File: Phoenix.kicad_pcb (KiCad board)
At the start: 2 copper layers, 83.2 x 37.6 mm, 88 parts, among them J1 Mini USB Female, J2 Battery Connector, J3 Pyro Connectors, Q1 2N7000, Q2 BSS84, Q3 IRFML8244TRPBF, Q4 IRFML8244TRPBF, Q5 IRFML8244TRPBF, Q6 IRFML8244TRPBF, U1 RP2040, U3 AMS1117-3.3, U4 I3G4250D, U5 MS5637-02BA03, U6 ADXL343, U8 Si4468/7, U9 L70B-M39, Y1 12MHz, Y2 30MHz

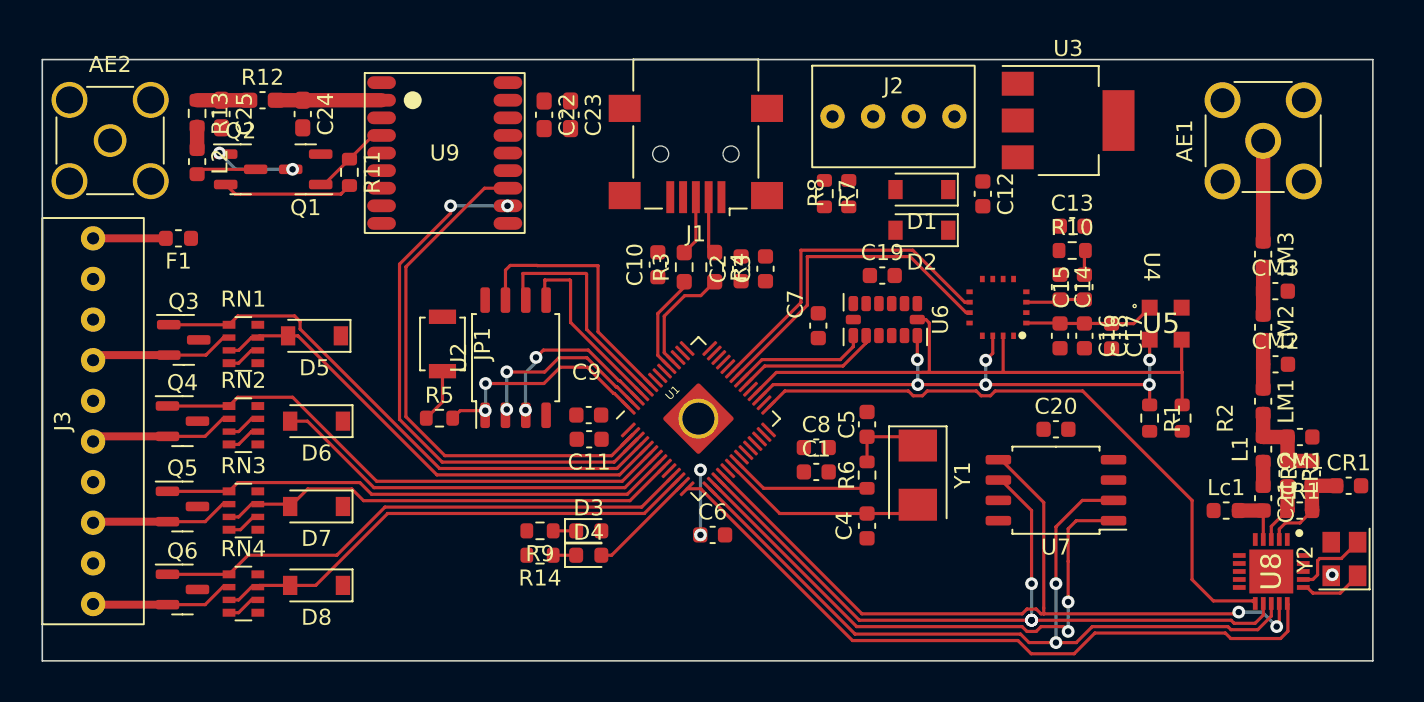
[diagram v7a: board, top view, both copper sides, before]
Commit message: Added fills
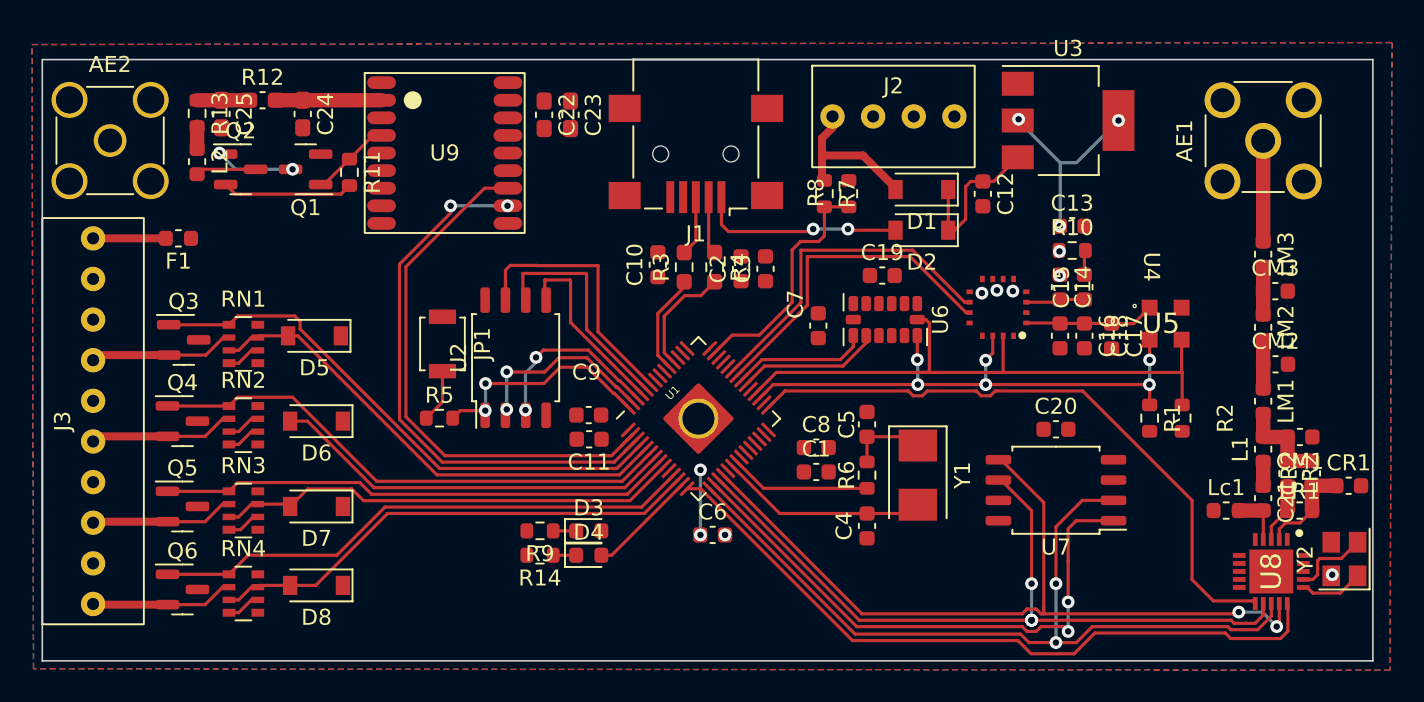
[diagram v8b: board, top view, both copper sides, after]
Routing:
- net /Power Supply/VBat/4: track 0.00 -> 15.6 mm
- net VBUS: track 0.00 -> 12.9 mm, vias 0 -> 2
- net +3V3: track 4.08 -> 16.9 mm, vias 2 -> 5
- net Net-(C12-Pad1): track 0.00 -> 9.97 mm
- net +BATT: track 0.00 -> 9.92 mm
- net GND: vias 1 -> 7
- added copper zone on B.Cu, net GND
- added copper zone on F.Cu, net GND
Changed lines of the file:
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@@
   (segment (start 139.446 37.1915) (end 139.446 30.8925) (width 0.9) (layer "F.Cu") (net 1))
   (segment (start 76.025 28.3545) (end 72.797 28.3545) (width 0.9) (layer "F.Cu") (net 2))
+  (via (at 126.711526 37.80667) (size 0.8) (drill 0.4) (layers "F.Cu" "B.Cu") (net 4))
+  (via (at 121.861299 40.415582) (size 0.8) (drill 0.4) (layers "F.Cu" "B.Cu") (free) (net 4))
   (via (at 143.764 58.0195) (size 0.8) (drill 0.4) (layers "F.Cu" "B.Cu") (net 4))
+  (via (at 126.723013 39.323004) (size 0.8) (drill 0.4) (layers "F.Cu" "B.Cu") (net 4))
+  (via (at 122.800711 40.236889) (size 0.8) (drill 0.4) (layers "F.Cu" "B.Cu") (free) (net 4))
+  (via (at 123.796284 40.287944) (size 0.8) (drill 0.4) (layers "F.Cu" "B.Cu") (free) (net 4))
+  (via (at 105.804 55.5305) (size 0.8) (drill 0.4) (layers "F.Cu" "B.Cu") (free) (net 4))
   (segment (start 104.254 55.5305) (end 104.267 55.5305) (width 0.2) (layer "F.Cu") (net 5))
+  (segment (start 126.537926 36.031426) (end 126.733 36.2265) (width 0.2) (layer "F.Cu") (net 5))
+  (via (at 126.733 36.2265) (size 0.8) (drill 0.4) (layers "F.Cu" "B.Cu") (net 5))
+  (via (at 130.404 29.6225) (size 0.8) (drill 0.4) (layers "F.Cu" "B.Cu") (net 5))
+  (via (at 124.155693 29.544612) (size 0.8) (drill 0.4) (layers "F.Cu" "B.Cu") (net 5))
   (via (at 104.267 55.5305) (size 0.8) (drill 0.4) (layers "F.Cu" "B.Cu") (net 5))
   (via (at 104.267 51.4665) (size 0.8) (drill 0.4) (layers "F.Cu" "B.Cu") (net 5))
+  (segment (start 126.761241 32.259746) (end 127.766754 32.259746) (width 0.2) (layer "B.Cu") (net 5))
+  (segment (start 124.155693 29.544612) (end 124.155693 29.654198) (width 0.2) (layer "B.Cu") (net 5))
+  (segment (start 124.155693 29.654198) (end 126.761241 32.259746) (width 0.2) (layer "B.Cu") (net 5))
   (segment (start 104.267 55.5305) (end 104.267 51.4665) (width 0.2) (layer "B.Cu") (net 5))
+  (segment (start 126.761241 36.198259) (end 126.733 36.2265) (width 0.2) (layer "B.Cu") (net 5))
+  (segment (start 127.766754 32.259746) (end 130.404 29.6225) (width 0.2) (layer "B.Cu") (net 5))
+  (segment (start 126.761241 32.259746) (end 126.761241 36.198259) (width 0.2) (layer "B.Cu") (net 5))
   (segment (start 114.681 54.1925) (end 109.223972 54.1925) (width 0.2) (layer "F.Cu") (net 6))
   (segment (start 117.306 54.1925) (end 114.681 54.1925) (width 0.2) (layer "F.Cu") (net 6))
@@
   (segment (start 140.9705 50.907) (end 140.97 50.9075) (width 0.9) (layer "F.Cu") (net 8))
   (segment (start 142.494 50.907) (end 140.9705 50.907) (width 0.9) (layer "F.Cu") (net 8))
+  (segment (start 112.522 29.3685) (end 112.522 30.070541) (width 0.5) (layer "F.Cu") (net 9))
+  (segment (start 116.46 33.838447) (end 114.429233 31.80768) (width 0.5) (layer "F.Cu") (net 9))
+  (segment (start 111.999651 31.80768) (end 111.870419 31.936912) (width 0.5) (layer "F.Cu") (net 9))
+  (segment (start 114.429233 31.80768) (end 111.999651 31.80768) (width 0.5) (layer "F.Cu") (net 9))
+  (segment (start 111.870419 31.936912) (end 111.870419 33.225919) (width 0.5) (layer "F.Cu") (net 9))
+  (segment (start 116.46 33.9405) (end 116.46 33.838447) (width 0.5) (layer "F.Cu") (net 9))
+  (segment (start 111.870419 30.722122) (end 111.870419 31.936912) (width 0.5) (layer "F.Cu") (net 9))
+  (segment (start 112.522 30.070541) (end 111.870419 30.722122) (width 0.5) (layer "F.Cu") (net 9))
+  (segment (start 111.870419 33.225919) (end 112.014 33.3695) (width 0.5) (layer "F.Cu") (net 9))
+  (segment (start 111.15942 36.563455) (end 106.018186 36.563455) (width 0.2) (layer "F.Cu") (net 10))
+  (segment (start 116.46 36.4805) (end 113.559098 36.4805) (width 0.2) (layer "F.Cu") (net 10))
+  (segment (start 111.3145 36.408375) (end 111.15942 36.563455) (width 0.2) (layer "F.Cu") (net 10))
+  (segment (start 106.018186 36.563455) (end 105.578499 36.123768) (width 0.2) (layer "F.Cu") (net 10))
+  (segment (start 105.578499 36.123768) (end 105.578499 34.4135) (width 0.2) (layer "F.Cu") (net 10))
+  (segment (start 113.559098 36.4805) (end 113.486973 36.408375) (width 0.2) (layer "F.Cu") (net 10))
+  (via (at 111.3145 36.408375) (size 0.8) (drill 0.4) (layers "F.Cu" "B.Cu") (net 10))
+  (via (at 113.486973 36.408375) (size 0.8) (drill 0.4) (layers "F.Cu" "B.Cu") (net 10))
+  (segment (start 113.486973 36.408375) (end 111.3145 36.408375) (width 0.2) (layer "B.Cu") (net 10))
   (segment (start 95.059 55.2765) (end 96.4945 55.2765) (width 0.2) (layer "F.Cu") (net 11))
   (segment (start 105.156 37.8775) (end 104.778499 37.499999) (width 0.2) (layer "F.Cu") (net 12))
@@
   (segment (start 81.534 56.8005) (end 75.986 56.8005) (width 0.2) (layer "F.Cu") (net 51))
   (segment (start 102.584365 51.795534) (end 100.589399 53.7905) (width 0.2) (layer "F.Cu") (net 51))
+  (segment (start 109.997837 40.987949) (end 107.945472 43.040314) (width 0.2) (layer "F.Cu") (net 54))
+  (segment (start 112.014 35.0195) (end 112.014 36.834562) (width 0.2) (layer "F.Cu") (net 54))
+  (segment (start 112.014 36.834562) (end 111.662504 37.186058) (width 0.2) (layer "F.Cu") (net 54))
+  (segment (start 112.014 35.0195) (end 113.538 35.0195) (width 0.2) (layer "F.Cu") (net 54))
+  (segment (start 110.525709 37.186058) (end 109.997837 37.71393) (width 0.2) (layer "F.Cu") (net 54))
+  (segment (start 111.662504 37.186058) (end 110.525709 37.186058) (width 0.2) (layer "F.Cu") (net 54))
+  (segment (start 109.997837 37.71393) (end 109.997837 40.987949) (width 0.2) (layer "F.Cu") (net 54))
+  (segment (start 107.945472 43.040314) (end 106.248416 43.040314) (width 0.2) (layer "F.Cu") (net 54))
+  (segment (start 106.248416 43.040314) (end 104.839614 44.449116) (width 0.2) (layer "F.Cu") (net 54))
   (segment (start 74.792 43.9925) (end 75.392 43.9925) (width 0.2) (layer "F.Cu") (net 59))
   (segment (start 75.392 43.9925) (end 76.192 43.1925) (width 0.2) (layer "F.Cu") (net 59))
@@
   (segment (start 124.64 40.9815) (end 126.576 40.9815) (width 0.2) (layer "F.Cu") (net 81))
   (segment (start 126.576 40.9815) (end 126.746 40.8115) (width 0.2) (layer "F.Cu") (net 81))
+  (segment (start 121.92 33.4325) (end 122.594 33.4325) (width 0.2) (layer "F.Cu") (net 82))
+  (segment (start 119.76 36.4805) (end 120.158845 36.4805) (width 0.2) (layer "F.Cu") (net 82))
+  (segment (start 121.162092 33.4325) (end 121.92 33.4325) (width 0.2) (layer "F.Cu") (net 82))
+  (segment (start 119.76 36.4805) (end 119.76 33.9405) (width 0.2) (layer "F.Cu") (net 82))
+  (segment (start 120.158845 36.4805) (end 120.848089 35.791256) (width 0.2) (layer "F.Cu") (net 82))
+  (segment (start 122.594 33.4325) (end 124.104 31.9225) (width 0.2) (layer "F.Cu") (net 82))
+  (segment (start 120.848089 35.791256) (end 120.848089 33.746503) (width 0.2) (layer "F.Cu") (net 82))
+  (segment (start 120.848089 33.746503) (end 121.162092 33.4325) (width 0.2) (layer "F.Cu") (net 82))
   (segment (start 98.0695 56.8005) (end 98.710771 56.8005) (width 0.2) (layer "F.Cu") (net 83))
   (segment (start 98.710771 56.8005) (end 103.150051 52.361219) (width 0.2) (layer "F.Cu") (net 83))
@@
   (segment (start 101.6 41.6875) (end 101.6 44.305787) (width 0.2) (layer "F.Cu") (net 94))
   (segment (start 70.8405 36.9885) (end 66.294 36.9885) (width 0.5) (layer "F.Cu") (net 95))
+  (zone (net 4) (net_name "GND") (layers F&B.Cu) (hatch edge 0.508)
+    (connect_pads (clearance 0.2))
+    (min_thickness 0.2) (filled_areas_thickness no)
+    (fill yes (thermal_gap 0.5) (thermal_bridge_width 0.5))
+    (polygon
+      (pts
+        (xy 147.38112 63.990324)
+        (xy 62.56838 63.900809)
+        (xy 62.473783 24.871991)
+        (xy 147.504728 24.750331)
+      )
+    )
+  )
 )
